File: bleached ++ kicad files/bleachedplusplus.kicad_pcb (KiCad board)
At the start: 2 copper layers, 126 x 46 mm, 14 parts, among them U1 Teensy-LC_minimal

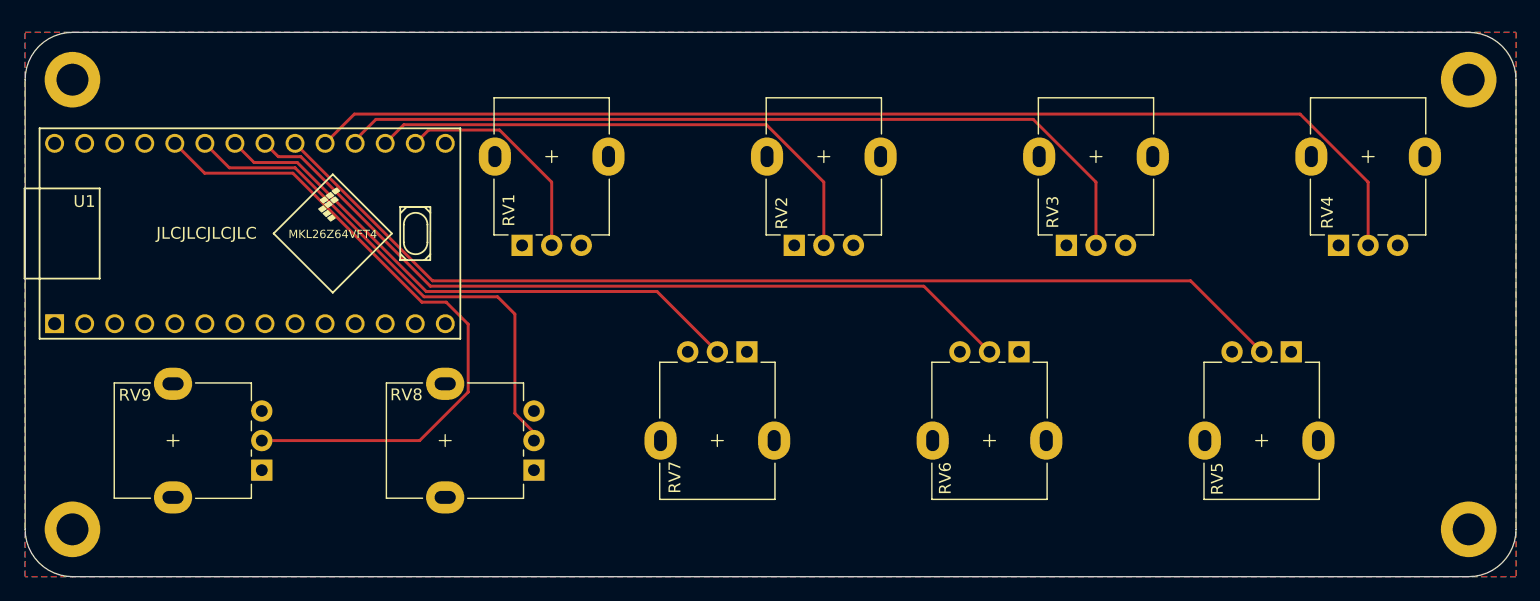
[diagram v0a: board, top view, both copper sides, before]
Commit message: Add files via upload
fixed potentiometer rotation
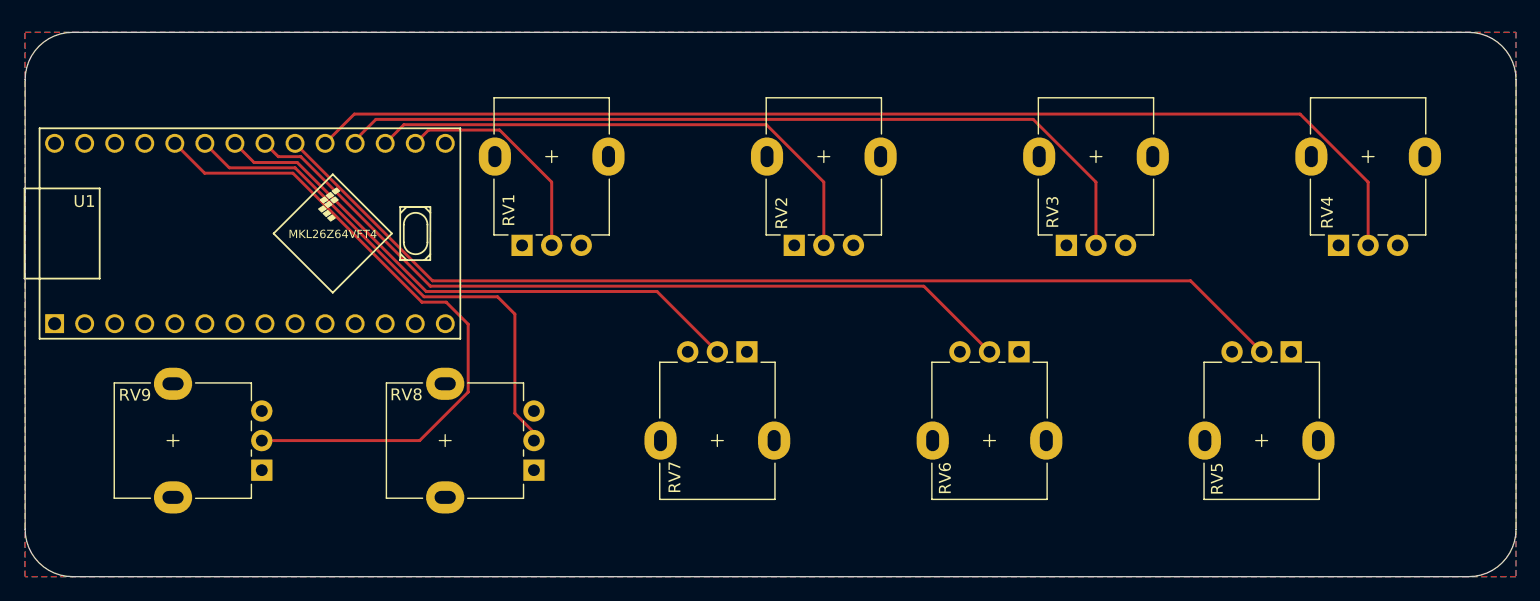
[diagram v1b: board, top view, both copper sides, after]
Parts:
- removed REF** (x4): MountingHole_2.7mm_M2.5_DIN965_Pad, MountingHole:MountingHole_2.7mm_M2.5_DIN965_Pad
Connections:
- RV1 pad 1: +3V3 -> GND
- RV1 pad 3: GND -> +3V3
- RV2 pad 1: +3V3 -> GND
- RV2 pad 3: GND -> +3V3
- RV3 pad 1: +3V3 -> GND
- RV3 pad 3: GND -> +3V3
- RV4 pad 1: +3V3 -> GND
- RV4 pad 3: GND -> +3V3
- RV5 pad 1: +3V3 -> GND
- RV5 pad 3: GND -> +3V3
- RV6 pad 1: +3V3 -> GND
- RV6 pad 3: GND -> +3V3
- RV7 pad 1: +3V3 -> GND
- RV7 pad 3: GND -> +3V3
- RV8 pad 1: +3V3 -> GND
- RV8 pad 3: GND -> +3V3
- RV9 pad 1: +3V3 -> GND
- RV9 pad 3: GND -> +3V3
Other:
- board text removed: "JLCJLCJLCJLC"

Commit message: Add files via upload
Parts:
- added H1: MountingHole_2.7mm_M2.5_DIN965_Pad, MountingHole:MountingHole_2.7mm_M2.5_DIN965_Pad, F.Cu at (64.0, 78.0)
- added H2: MountingHole_2.7mm_M2.5_DIN965_Pad, MountingHole:MountingHole_2.7mm_M2.5_DIN965_Pad, F.Cu at (64.0, 116.0)
- added H3: MountingHole_2.7mm_M2.5_DIN965_Pad, MountingHole:MountingHole_2.7mm_M2.5_DIN965_Pad, F.Cu at (182.0, 116.0)
- added H4: MountingHole_2.7mm_M2.5_DIN965_Pad, MountingHole:MountingHole_2.7mm_M2.5_DIN965_Pad, F.Cu at (182.0, 78.0)

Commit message: Add files via upload
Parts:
- H1, H2, H3, H4: value MountingHole_2.7mm_M2.5_DIN965_Pad -> MountingHole
- RV1, RV2, RV3, RV4, RV5, RV6, RV7, RV8, RV9: footprint Potentiometer_THT:mypot -> Potentiometer_THT:Potentiometer_Alpha_RD901F-40-00D_Single_Vertical
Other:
- board text added: "JLCJLCJLCJLC"
